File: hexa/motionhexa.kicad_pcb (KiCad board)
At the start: 4 copper layers, 78 x 67.5 mm, 297 parts, among them J1 Conn_01x04_Socket

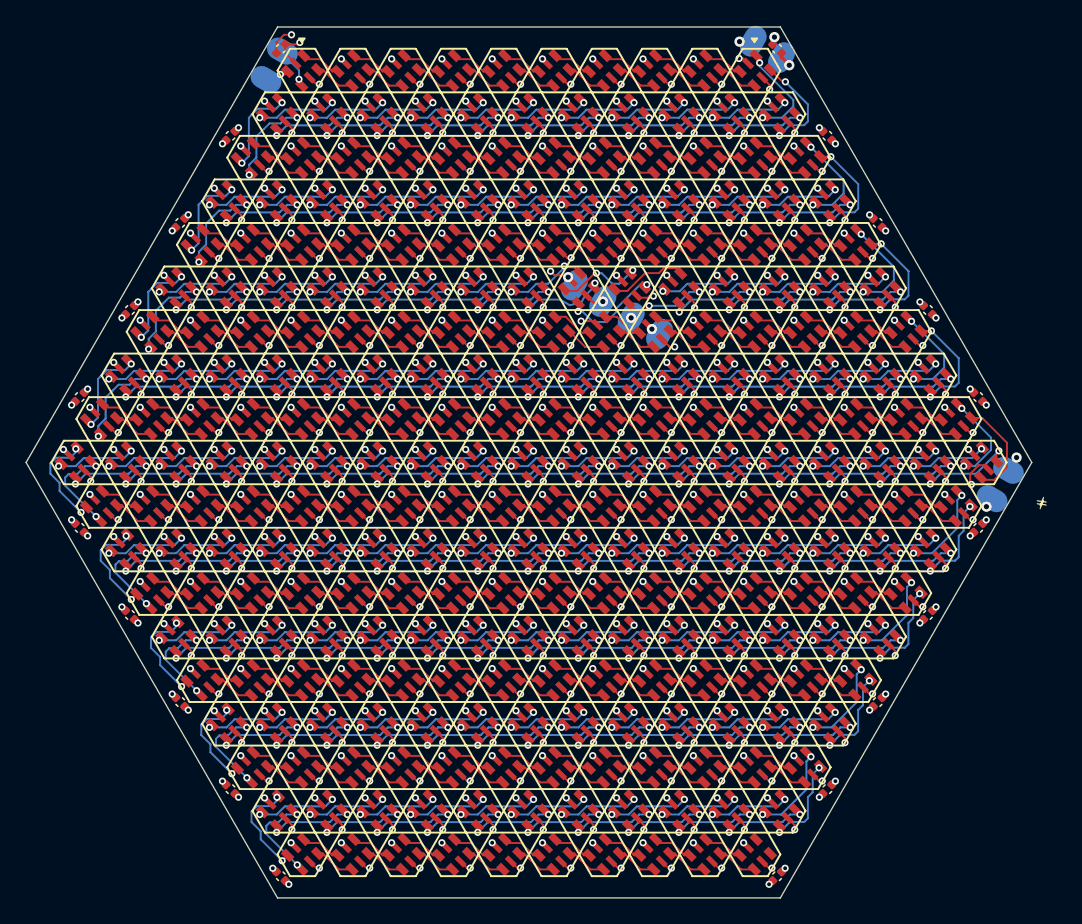
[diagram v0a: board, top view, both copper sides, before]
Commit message: move hexa capacitors farther away from board edges for case mechanical clearance
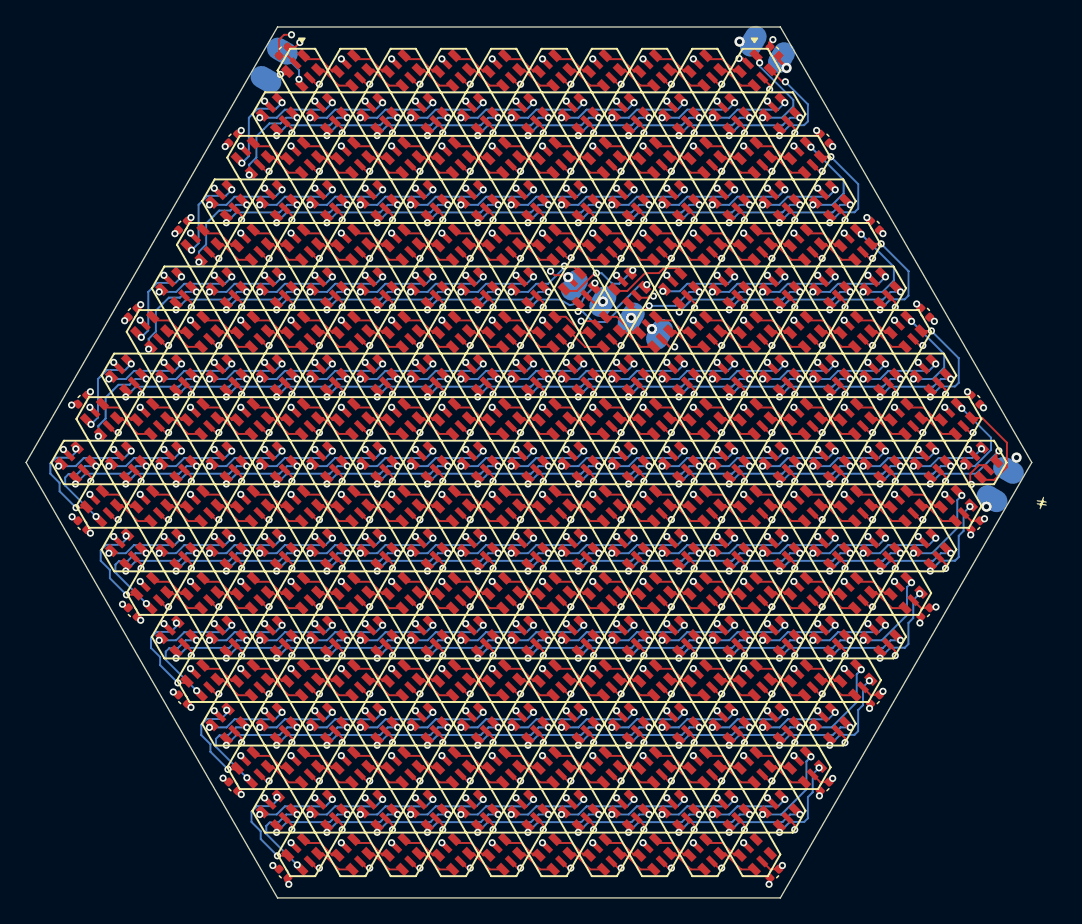
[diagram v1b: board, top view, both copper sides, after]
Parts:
- moved C18 0.30 mm to (122.9, 125.1)
- moved C11 0.30 mm to (65.4, 104.9)
- moved C13 0.30 mm to (69.3, 111.6)
- moved C14 0.30 mm to (130.7, 111.6)
- moved C15 0.30 mm to (73.2, 118.4)
- moved C16 0.30 mm to (126.8, 118.4)
- moved C17 0.30 mm to (77.1, 125.1)
- moved C4 0.30 mm to (122.9, 74.9)
- moved C9 0.30 mm to (65.4, 95.1)
- moved C1 0.30 mm to (81.0, 68.1)
- moved C10 0.30 mm to (134.6, 95.1)
- moved C12 0.30 mm to (134.6, 104.9)
- moved C19 0.30 mm to (81.0, 131.9)
- moved C2 0.30 mm to (119.0, 68.1)
- moved C20 0.30 mm to (119.0, 131.9)
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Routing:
- net +5V: track 298.5 -> 302.3 mm, vias 292 -> 287

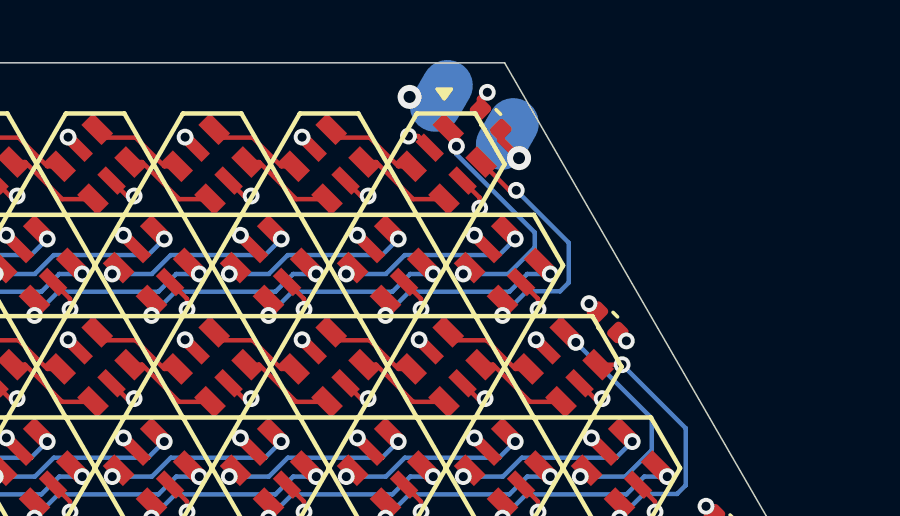
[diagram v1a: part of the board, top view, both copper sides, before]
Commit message: add photosensor back in, but on the front of the hexa
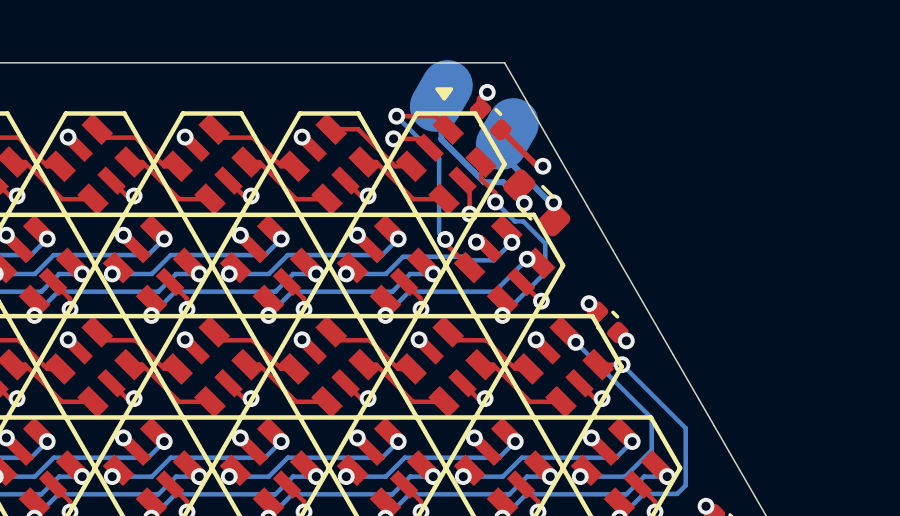
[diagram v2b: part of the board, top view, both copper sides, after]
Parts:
- added Q1: Q_Photo_NPN, Resistor_SMD:R_0603_1608Metric, F.Cu at (120.6, 70.9)
- J1: value Conn_01x04_Socket -> Conn_01x06_Socket
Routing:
- net /PHOTOSENSOR_PWR: track 0.00 -> 5.76 mm, vias 0 -> 1
- net /PHOTOSENSOR_READ: track 0.00 -> 3.59 mm, vias 0 -> 1
- net Net-(D10-CKO): track 8.52 -> 7.25 mm
- net GND: track 172.5 -> 171.6 mm, vias 294 -> 293
- net Net-(D11-CKO): track 7.06 -> 6.28 mm
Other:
- board text added: "PHOTO"
